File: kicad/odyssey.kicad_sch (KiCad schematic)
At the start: 8 parts, among them J1 MSD-4-A, U1 I3G4250DTR, U2 IIS2MDCTR, U3 XIAO-RP2040-SMD, U4 TL3305AF260QG, U5 MPL3115A2

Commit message: feat: shrink board and autoroute
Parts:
- removed U4: TL3305AF260QG, footprints:SW_TL3305AF260QG, symbol TL3305AF260QG:TL3305AF260QG

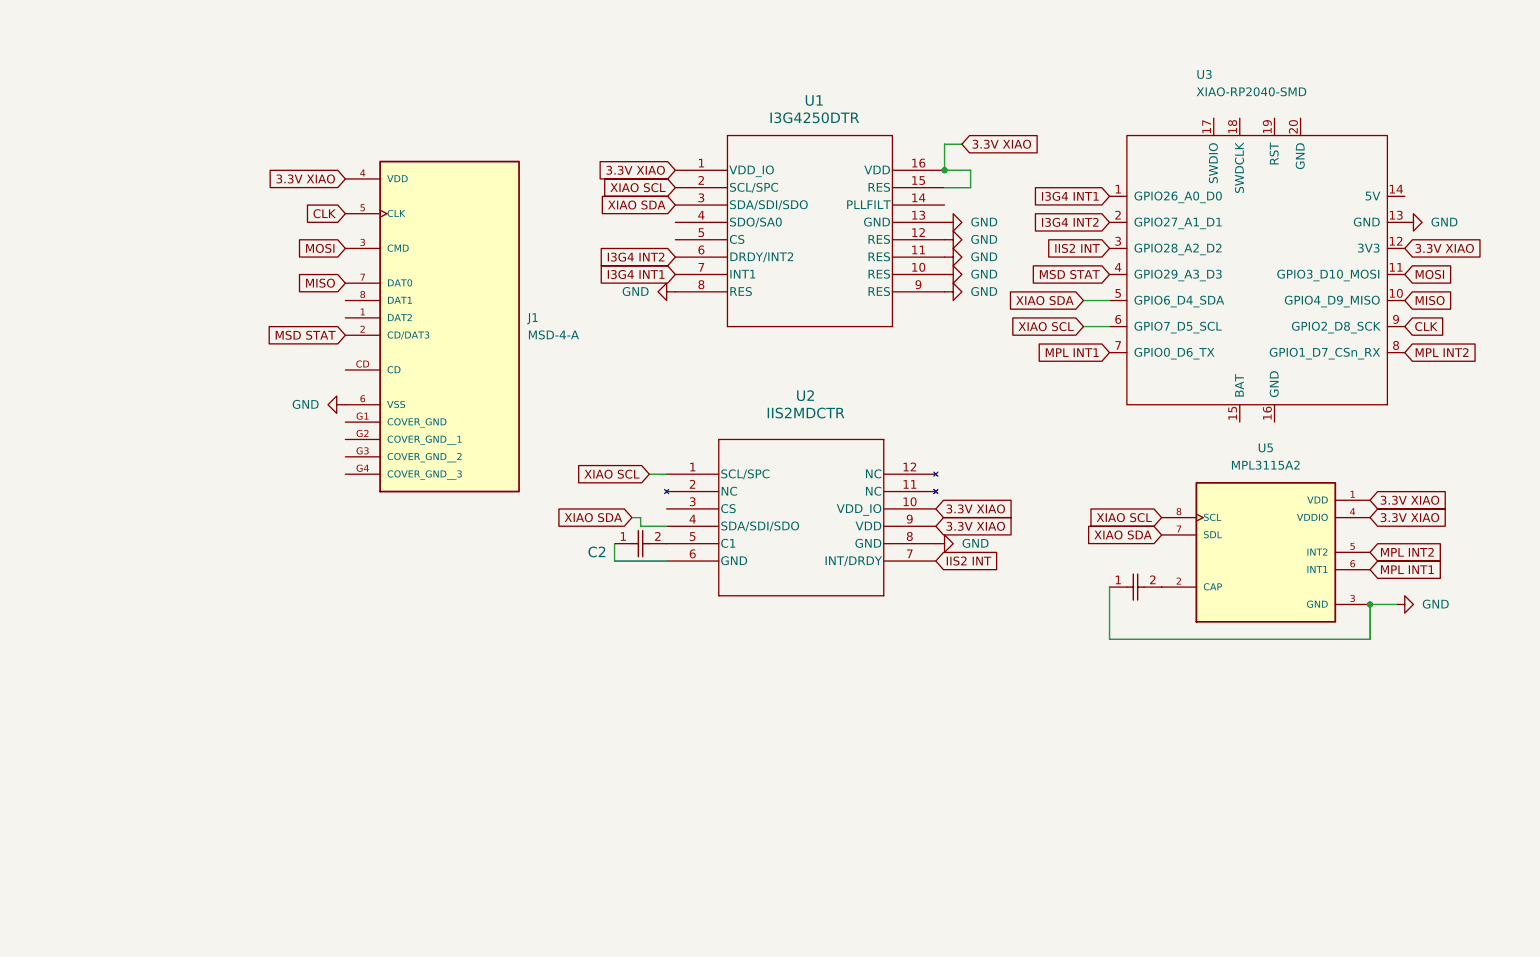
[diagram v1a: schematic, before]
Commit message: updating pcb
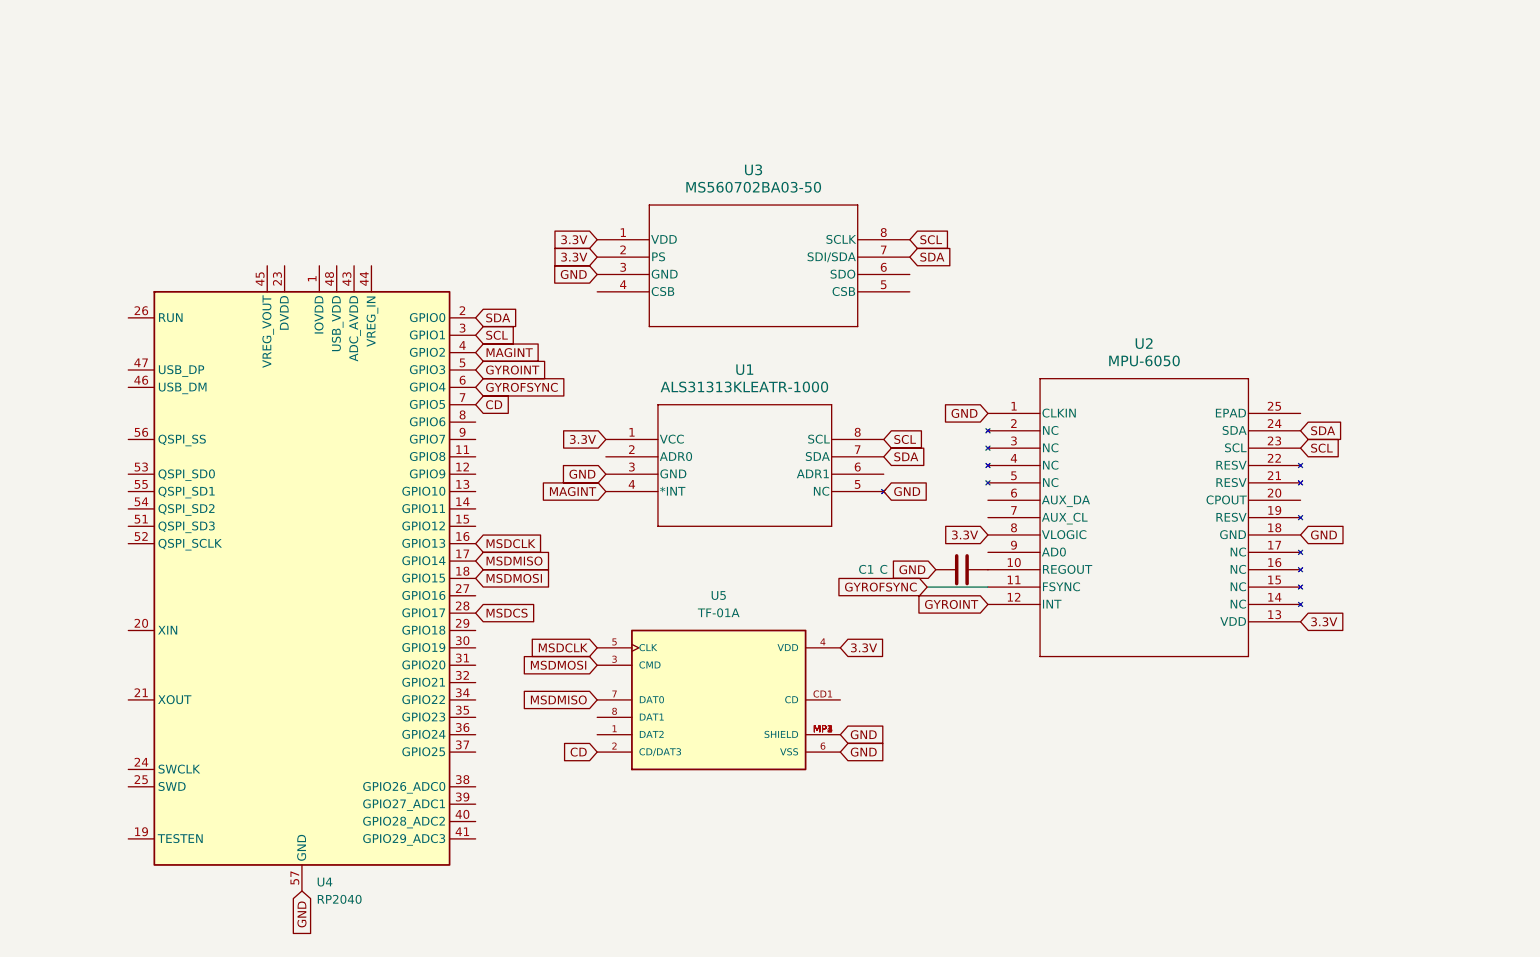
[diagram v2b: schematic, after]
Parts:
- removed C1: 0402B104K160CT, footprints:CAP_0402_N_WAL, symbol CAP:0402B104K160CT
- removed C3: C2, footprints:CAP_0402_N_WAL, symbol CAP:0402B104K160CT
- removed J1: MSD-4-A, footprints:CUI_MSD-4-A, symbol MSD-4-A:MSD-4-A
- removed U1: I3G4250DTR, footprints:I3G4250DTR, symbol I3G4250DTR:I3G4250DTR
- removed U2: IIS2MDCTR, footprints:IIS2MDCTR, symbol IIS2MDCTR:IIS2MDCTR
- removed U3: XIAO-RP2040-SMD, footprints:XIAO-RP2040-SMD, symbol Seeed_Studio_XIAO_Series:XIAO-RP2040-SMD
- removed U5: MPL3115A2, Package_LGA:NXP_LGA-8_3x5mm_P1.25mm_H1.1mm, symbol MPL3115A2:MPL3115A2
- added C1: C, Capacitor_SMD:C_0402_1005Metric, symbol Device:C
- added U1: ALS31313KLEATR-1000, footprints:TSSOP8_LE_ALM, symbol ALS31313KLEATR-1000:ALS31313KLEATR-1000
- added U2: MPU-6050, footprints:QFN24_4X4X0P9-0P5_TDK, symbol MPU-6050:MPU-6050
- added U3: MS560702BA03-50, footprints:SON8_MS5611_TEC, symbol MS560702BA03-50:MS560702BA03-50
- added U4: RP2040, footprints:IC57_RP2040, symbol MCU_RaspberryPi:RP2040
- added U5: TF-01A, footprints:TF-01A, symbol TF-01A:TF-01A
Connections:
- net GND: now also C1.1, U1.3 (GND), U1.5 (NC), U2.1 (CLKIN), U2.18 (GND), U3.3 (GND), U4.57 (GND), U5.6 (VSS), U5.MP1 (SHIELD), U5.MP2 (SHIELD), U5.MP3 (SHIELD), U5.MP4 (SHIELD)
- new net: C1.2, U2.10 (REGOUT)
- new net: U4.1 (IOVDD), U4.10 (IOVDD), U4.22 (IOVDD), U4.33 (IOVDD), U4.42 (IOVDD), U4.49 (IOVDD)
- new net: U4.23 (DVDD), U4.50 (DVDD)
- new net 3.3V: U1.1 (VCC), U2.13 (VDD), U2.8 (VLOGIC), U3.1 (VDD), U3.2 (PS), U5.4 (VDD)
- new net CD: U4.7 (GPIO5), U5.2 (CD/DAT3)
- new net GYROFSYNC: U2.11 (FSYNC), U4.6 (GPIO4)
- new net GYROINT: U2.12 (INT), U4.5 (GPIO3)
- new net MAGINT: U1.4 (*INT), U4.4 (GPIO2)
- new net MSDCLK: U4.16 (GPIO13), U5.5 (CLK)
- new net MSDCS: U4.28 (GPIO17)
- new net MSDMISO: U4.17 (GPIO14), U5.7 (DAT0)
- new net MSDMOSI: U4.18 (GPIO15), U5.3 (CMD)
- new net SCL: U1.8 (SCL), U2.23 (SCL), U3.8 (SCLK), U4.3 (GPIO1)
- new net SDA: U1.7 (SDA), U2.24 (SDA), U3.7 (SDI/SDA), U4.2 (GPIO0)

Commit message: trying firmware stuff
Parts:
- removed U4: RP2040, footprints:IC57_RP2040, symbol MCU_RaspberryPi:RP2040
- added C2: C, Capacitor_SMD:C_0402_1005Metric, symbol Device:C
- added U4: XIAO-RP2040-SMD, footprints:XIAO-RP2040-SMD, symbol Seeed_Studio_XIAO_Series:XIAO-RP2040-SMD
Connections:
- net 3.3V: now also U4.12 (3V3)
- net GND: now also U1.2 (ADR0), U1.6 (ADR1), U2.9 (AD0), U3.6 (SDO), C2.1, U4.13 (GND)
- net GYROFSYNC: now also U4.3 (GPIO28_A2_D2)
- net GYROINT: now also U4.2 (GPIO27_A1_D1)
- net MAGINT: now also U4.1 (GPIO26_A0_D0)
- net MSDCLK: now also U4.9 (GPIO2_D8_SCK)
- net MSDMISO: now also U4.10 (GPIO4_D9_MISO)
- net MSDMOSI: now also U4.11 (GPIO3_D10_MOSI)
- net SCL: now also U4.6 (GPIO7_D5_SCL)
- net SDA: now also U4.5 (GPIO6_D4_SDA)
- net at U2.20 (CPOUT): now also C2.2
- net CD renamed MSDCD
- net MSDCD: now also U4.4 (GPIO29_A3_D3)
